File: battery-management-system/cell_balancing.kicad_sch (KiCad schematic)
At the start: 30 parts, among them J22 BALANCE_INPUTS, J23 BALANCE_CURRENT, J27 BALANCE_CONTROL, Q11 DMN3404L, Q12 DMN3730U, Q14 DMN3730U, Q15 DMN3730U, Q16 DMN3730U, Q17 DMN3730U, SW1 CELL1_MINUS, SW2 CELL1_PLUS, SW3 CELL2_MINUS, SW4 CELL2_PLUS, SW5 CELL3_PLUS, SW6 CELL3_MINUS, SW7 CELL4_PLUS, SW8 CELL4_MINUS, U13 MC74VHC139

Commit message: improve layout
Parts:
- renumbered C33 to C45, C30 to C46, C31 to C47, C32 to C48, D16 to D22, D17 to D23, D18 to D24, D19 to D25, J27 to J26, J22 to J27, J23 to J28, Q12 to Q14, Q11 to Q15, Q14 to Q16, Q15 to Q17, Q16 to Q18, Q17 to Q19, R50 to R61, R49 to R62, R48 to R63, SW7 to SW1, SW8 to SW2, SW5 to SW3, SW6 to SW4, SW4 to SW5, SW3 to SW6, SW2 to SW7, SW1 to SW8, U13 to U16

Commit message: add project for DC DC converter PCB
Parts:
- C46, C47, C48: RS order number 875-6720 -> 875-6720
- Q15: RS order number 751-4171 -> 751-4171
- R63: RS order number 796-2431 -> 796-2431
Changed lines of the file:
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@@
       (effects (font (size 1.27 1.27)) hide)
     )
-    (property "RS order number" " 796-2431" (at 160.02 137.16 0)
+    (property "RS order number" "796-2431" (at 160.02 137.16 0)
       (effects (font (size 1.27 1.27)) hide)
     )
@@
       (effects (font (size 1.27 1.27)) hide)
     )
-    (property "RS order number" "    875-6720" (at 238.506 146.05 0)
+    (property "RS order number" "875-6720" (at 238.506 146.05 0)
       (effects (font (size 1.27 1.27)) hide)
     )
@@
       (effects (font (size 1.27 1.27)) hide)
     )
-    (property "RS order number" " 751-4171" (at 156.21 140.97 0)
+    (property "RS order number" "751-4171" (at 156.21 140.97 0)
       (effects (font (size 1.27 1.27)) hide)
     )
@@
       (effects (font (size 1.27 1.27)) hide)
     )
-    (property "RS order number" "    875-6720" (at 263.906 146.05 0)
+    (property "RS order number" "875-6720" (at 263.906 146.05 0)
       (effects (font (size 1.27 1.27)) hide)
     )
@@
       (effects (font (size 1.27 1.27)) hide)
     )
-    (property "RS order number" "    875-6720" (at 251.206 146.05 0)
-      (effects (font (size 1.27 1.27)) hide)
-    )
+    (property "RS order number" "875-6720" (at 251.206 146.05 0)
+      (effects (font (size 1.27 1.27)) hide)
+    )

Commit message: update footprints and layout
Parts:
- removed C48: 90F, benediktibk:vishay_super_cap_form_g, symbol benediktibk:C_90F_THT_4_2V
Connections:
- net BALANCE_CAP_MINUS_RAW: now also C46.2, C47.2; no longer C46.1, C47.1
- net BALANCE_CAP_PLUS_RAW: now also C46.1, C47.1; no longer C46.2, C46.3, C47.2, C47.3
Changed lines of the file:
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@@
 (kicad_sch (version 20230121) (generator eeschema)
   (paper "A4")
-  (junction (at 234.95 137.16) (diameter 0) (color 0 0 0 0)
-  )
   (junction (at 87.63 154.94) (diameter 0) (color 0 0 0 0)
   )
   (junction (at 44.45 80.01) (diameter 0) (color 0 0 0 0)
   )
-  (junction (at 246.38 154.94) (diameter 0) (color 0 0 0 0)
-  )
   (junction (at 194.31 154.94) (diameter 0) (color 0 0 0 0)
   )
@@
   (junction (at 247.65 109.22) (diameter 0) (color 0 0 0 0)
   )
-  (junction (at 222.25 137.16) (diameter 0) (color 0 0 0 0)
-  )
   (junction (at 201.93 154.94) (diameter 0) (color 0 0 0 0)
   )
@@
   (junction (at 222.25 25.4) (diameter 0) (color 0 0 0 0)
   )
-  (junction (at 219.71 137.16) (diameter 0) (color 0 0 0 0)
-  )
   (junction (at 100.33 137.16) (diameter 0) (color 0 0 0 0)
   )
@@
   (junction (at 222.25 19.05) (diameter 0) (color 0 0 0 0)
   )
-  (junction (at 247.65 137.16) (diameter 0) (color 0 0 0 0)
+  (junction (at 220.98 137.16) (diameter 0) (color 0 0 0 0)
   )
   (junction (at 130.81 120.65) (diameter 0) (color 0 0 0 0)
@@
   (junction (at 171.45 154.94) (diameter 0) (color 0 0 0 0)
   )
-  (junction (at 245.11 137.16) (diameter 0) (color 0 0 0 0)
+  (junction (at 233.68 137.16) (diameter 0) (color 0 0 0 0)
   )
   (junction (at 247.65 60.96) (diameter 0) (color 0 0 0 0)
-  )
-  (junction (at 232.41 137.16) (diameter 0) (color 0 0 0 0)
   )
   (junction (at 97.79 154.94) (diameter 0) (color 0 0 0 0)
@@
   (no_connect (at 220.98 74.93))
   (no_connect (at 220.98 69.85))
-  (wire (pts (xy 234.95 137.16) (xy 234.95 143.51))
-    (stroke (width 0) (type default))
-  )
   (wire (pts (xy 67.31 34.29) (xy 67.31 38.1))
     (stroke (width 0) (type default))
@@
     (stroke (width 0) (type default))
   )
-  (wire (pts (xy 246.38 154.94) (xy 255.27 154.94))
+  (wire (pts (xy 233.68 154.94) (xy 255.27 154.94))
+    (stroke (width 0) (type default))
+  )
+  (wire (pts (xy 220.98 137.16) (xy 220.98 143.51))
+    (stroke (width 0) (type default))
+  )
+  (wire (pts (xy 233.68 137.16) (xy 255.27 137.16))
     (stroke (width 0) (type default))
   )
@@
     (stroke (width 0) (type default))
   )
-  (wire (pts (xy 245.11 137.16) (xy 234.95 137.16))
-    (stroke (width 0) (type default))
-  )
-  (wire (pts (xy 222.25 137.16) (xy 222.25 143.51))
-    (stroke (width 0) (type default))
-  )
-  (wire (pts (xy 247.65 137.16) (xy 247.65 143.51))
-    (stroke (width 0) (type default))
-  )
   (wire (pts (xy 194.31 69.85) (xy 200.66 69.85))
     (stroke (width 0) (type default))
@@
     (stroke (width 0) (type default))
   )
-  (wire (pts (xy 246.38 151.13) (xy 246.38 154.94))
-    (stroke (width 0) (type default))
-  )
   (wire (pts (xy 95.25 137.16) (xy 100.33 137.16))
     (stroke (width 0) (type default))
   )
-  (wire (pts (xy 245.11 137.16) (xy 245.11 143.51))
-    (stroke (width 0) (type default))
-  )
   (wire (pts (xy 67.31 53.34) (xy 67.31 57.15))
     (stroke (width 0) (type default))
@@
     (stroke (width 0) (type default))
   )
+  (wire (pts (xy 233.68 137.16) (xy 233.68 143.51))
+    (stroke (width 0) (type default))
+  )
   (wire (pts (xy 44.45 99.06) (xy 44.45 80.01))
     (stroke (width 0) (type default))
@@
     (stroke (width 0) (type default))
   )
-  (wire (pts (xy 232.41 137.16) (xy 222.25 137.16))
-    (stroke (width 0) (type default))
-  )
   (wire (pts (xy 147.32 25.4) (xy 182.88 25.4))
     (stroke (width 0) (type default))
   )
-  (wire (pts (xy 234.95 137.16) (xy 232.41 137.16))
-    (stroke (width 0) (type default))
-  )
   (wire (pts (xy 226.06 64.77) (xy 226.06 115.57))
     (stroke (width 0) (type default))
   )
+  (wire (pts (xy 220.98 137.16) (xy 233.68 137.16))
+    (stroke (width 0) (type default))
+  )
   (wire (pts (xy 72.39 22.86) (xy 100.33 22.86))
     (stroke (width 0) (type default))
@@
     (stroke (width 0) (type default))
   )
-  (wire (pts (xy 255.27 137.16) (xy 247.65 137.16))
-    (stroke (width 0) (type default))
-  )
   (wire (pts (xy 210.82 38.1) (xy 210.82 53.34))
     (stroke (width 0) (type default))
@@
     (stroke (width 0) (type default))
   )
-  (wire (pts (xy 100.33 137.16) (xy 219.71 137.16))
-    (stroke (width 0) (type default))
-  )
-  (wire (pts (xy 219.71 137.16) (xy 219.71 143.51))
+  (wire (pts (xy 100.33 137.16) (xy 220.98 137.16))
     (stroke (width 0) (type default))
   )
@@
     (stroke (width 0) (type default))
   )
-  (wire (pts (xy 232.41 137.16) (xy 232.41 143.51))
-    (stroke (width 0) (type default))
-  )
-  (wire (pts (xy 247.65 137.16) (xy 245.11 137.16))
-    (stroke (width 0) (type default))
-  )
   (wire (pts (xy 161.29 111.76) (xy 143.51 111.76))
     (stroke (width 0) (type default))
@@
     (stroke (width 0) (type default))
   )
-  (wire (pts (xy 219.71 137.16) (xy 222.25 137.16))
-    (stroke (width 0) (type default))
-  )
   (wire (pts (xy 90.17 99.06) (xy 90.17 137.16))
     (stroke (width 0) (type default))
@@
   )
   (wire (pts (xy 200.66 67.31) (xy 189.23 67.31))
-    (stroke (width 0) (type default))
-  )
-  (wire (pts (xy 233.68 154.94) (xy 246.38 154.94))
     (stroke (width 0) (type default))
   )
@@
     (effects (font (size 1.27 1.27)) (justify right))
   )
-  (netclass_flag "" (length 2.54) (shape round) (at 215.9 154.94 0) (fields_autoplaced)
-    (effects (font (size 1.27 1.27)) (justify left bottom))
-    (property "Netclass" "1A" (at 216.5985 152.4 0)
-      (effects (font (size 1.27 1.27) italic) (justify left))
-    )
-  )
   (netclass_flag "" (length 2.54) (shape round) (at 142.24 154.94 0) (fields_autoplaced)
     (effects (font (size 1.27 1.27)) (justify left bottom))
     (property "Netclass" "1A" (at 142.9385 152.4 0)
-      (effects (font (size 1.27 1.27) italic) (justify left))
-    )
-  )
-  (netclass_flag "" (length 2.54) (shape round) (at 214.63 137.16 0) (fields_autoplaced)
-    (effects (font (size 1.27 1.27)) (justify left bottom))
-    (property "Netclass" "1A" (at 215.3285 134.62 0)
       (effects (font (size 1.27 1.27) italic) (justify left))
     )
@@
     (effects (font (size 1.27 1.27)) (justify right bottom))
     (property "Netclass" "CONTROL_SIGNAL" (at 262.3185 87.63 0)
-      (effects (font (size 1.27 1.27) italic) (justify left))
-    )
-  )
-  (netclass_flag "" (length 2.54) (shape round) (at 184.15 154.94 0) (fields_autoplaced)
-    (effects (font (size 1.27 1.27)) (justify left bottom))
-    (property "Netclass" "1A" (at 184.8485 152.4 0)
       (effects (font (size 1.27 1.27) italic) (justify left))
     )
@@
       (effects (font (size 1.27 1.27)) hide)
     )
-    (pin "3")
     (pin "1")
     (pin "2")
@@
     )
   )
-  (symbol (lib_id "benediktibk:C_90F_THT_4_2V") (at 246.38 147.32 0) (unit 1)
-    (in_bom yes) (on_board yes) (dnp no) (fields_autoplaced)
-    (property "Reference" "C48" (at 251.46 144.907 0)
-      (effects (font (size 1.27 1.27)) (justify left))
-    )
-    (property "Value" "90F" (at 251.46 147.447 0)
-      (effects (font (size 1.27 1.27)) (justify left))
-    )
-    (property "Footprint" "benediktibk:vishay_super_cap_form_g" (at 247.3452 151.13 0)
-      (effects (font (size 1.27 1.27)) hide)
-    )
-    (property "Datasheet" "~" (at 246.38 147.32 0)
-      (effects (font (size 1.27 1.27)) hide)
-    )
-    (property "RS order number" "875-6720" (at 263.906 146.05 0)
-      (effects (font (size 1.27 1.27)) hide)
-    )
-    (pin "3")
-    (pin "1")
-    (pin "2")
-    (instances
-      (project "battery-management-system"
-        (path "/5272f0ff-3069-41a9-bca2-80beede8b4b2/3d1b4e38-a765-486c-a970-a0d54d5b41d9"
-          (reference "C48") (unit 1)
-        )
-      )
-    )
-  )
   (symbol (lib_id "benediktibk:SIL05-1A72-BV669") (at 67.31 137.16 0) (unit 1)
     (in_bom yes) (on_board yes) (dnp no)
@@
       (effects (font (size 1.27 1.27)) hide)
     )
-    (pin "3")
-    (pin "1")
-    (pin "2")
+    (pin "1")
+    (pin "2")

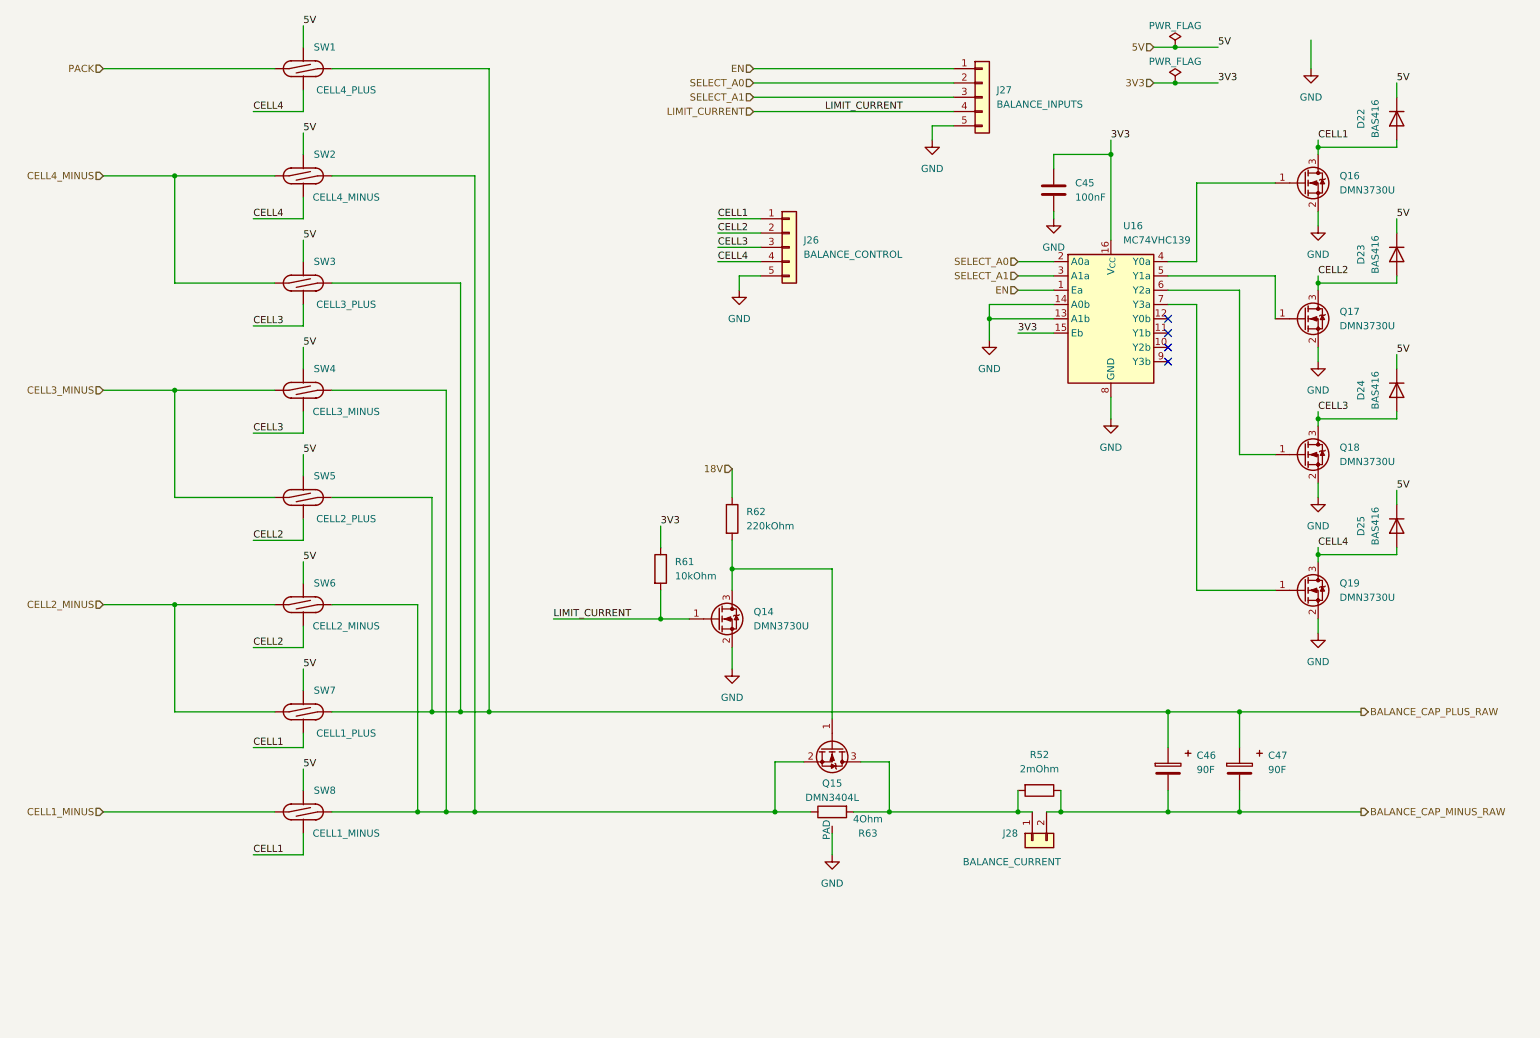
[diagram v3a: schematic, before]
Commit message: switch to inductor based cell balancing
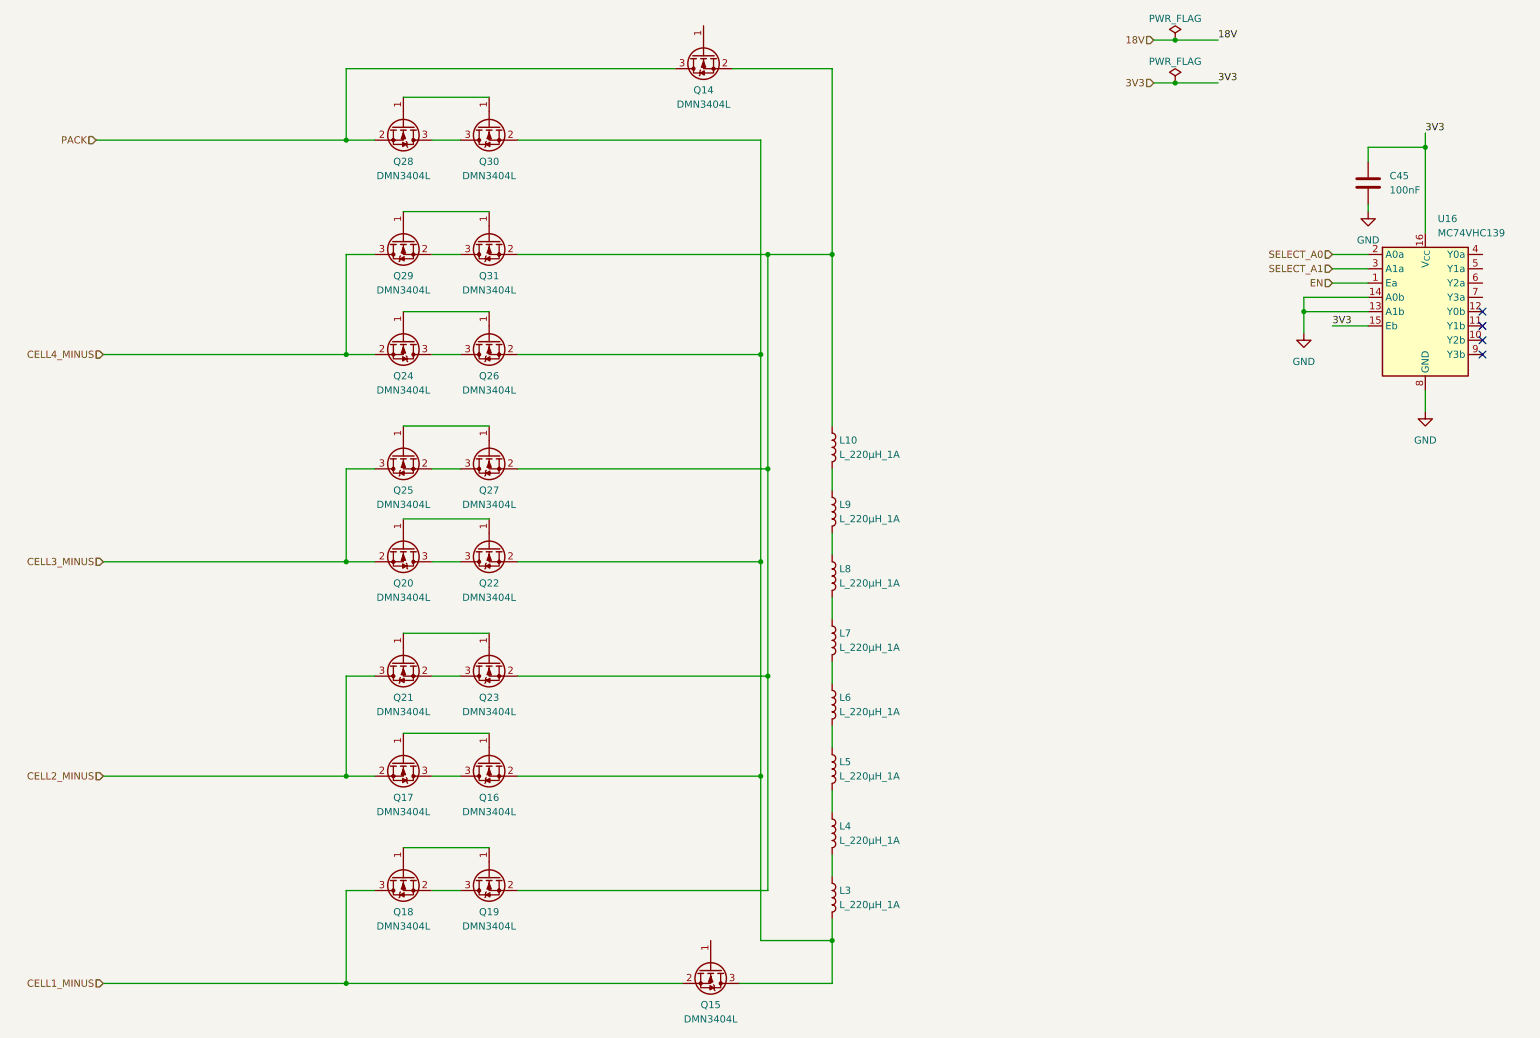
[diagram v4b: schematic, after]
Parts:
- removed C46, C47: 90F, benediktibk:vishay_super_cap_form_g, symbol benediktibk:C_90F_THT_4_2V
- removed D22, D23, D24, D25: BAS416, benediktibk:D_SOD-323, symbol benediktibk:BAS416
- removed J26: BALANCE_CONTROL, benediktibk:PinHeader_1x05_P2.54mm_Vertical, symbol benediktibk:Conn_01x05
- removed J27: BALANCE_INPUTS, benediktibk:PinHeader_1x05_P2.54mm_Vertical, symbol benediktibk:Conn_01x05
- removed J28: BALANCE_CURRENT, benediktibk:PinHeader_1x02_P2.54mm_Vertical, symbol benediktibk:Conn_01x02
- removed Q14, Q16, Q17, Q18, Q19: DMN3730U, benediktibk:SOT-23, symbol benediktibk:DMN3730U
- removed R52: 2mOhm, benediktibk:R_2512_6332Metric_Pad1.40x3.35mm_HandSolder, symbol benediktibk:R_2mOhm_SMD_2512_5W_1%
- removed R61: 10kOhm, benediktibk:R_0603_1608Metric_Pad0.98x0.95mm_HandSolder, symbol benediktibk:R_10kOhm_SMD_0603_100mW_1%
- removed R62: 220kOhm, benediktibk:R_0603_1608Metric_Pad0.98x0.95mm_HandSolder, symbol benediktibk:R_220kOhm_SMD_0603_100mW_1%
- removed R63: 4Ohm, benediktibk:TO-263-resistor, symbol benediktibk:R_4Ohm_SMD_35W_1%
- removed SW1: CELL4_PLUS, benediktibk:SIL05-1A72-BV669, symbol benediktibk:SIL05-1A72-BV669
- removed SW2: CELL4_MINUS, benediktibk:SIL05-1A72-BV669, symbol benediktibk:SIL05-1A72-BV669
- removed SW3: CELL3_PLUS, benediktibk:SIL05-1A72-BV669, symbol benediktibk:SIL05-1A72-BV669
- removed SW4: CELL3_MINUS, benediktibk:SIL05-1A72-BV669, symbol benediktibk:SIL05-1A72-BV669
- removed SW5: CELL2_PLUS, benediktibk:SIL05-1A72-BV669, symbol benediktibk:SIL05-1A72-BV669
- removed SW6: CELL2_MINUS, benediktibk:SIL05-1A72-BV669, symbol benediktibk:SIL05-1A72-BV669
- removed SW7: CELL1_PLUS, benediktibk:SIL05-1A72-BV669, symbol benediktibk:SIL05-1A72-BV669
- removed SW8: CELL1_MINUS, benediktibk:SIL05-1A72-BV669, symbol benediktibk:SIL05-1A72-BV669
- added L10, L3, L4, L5, L6, L7, L8, L9: L_220µH_1A, benediktibk:L_Wuerth_HCI-1050, symbol benediktibk:L_220µH_1A
- added Q14, Q16, Q17, Q18, Q19, Q20, Q21, Q22, Q23, Q24, Q25, Q26, Q27, Q28, Q29, Q30, Q31: DMN3404L, benediktibk:SOT-23, symbol benediktibk:DMN3404L
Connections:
- net CELL1_MINUS: now also Q15.2 (S), Q18.3 (D)
- net CELL2_MINUS: now also Q17.2 (S), Q21.3 (D)
- net CELL3_MINUS: now also Q20.2 (S), Q25.3 (D)
- net CELL4_MINUS: now also Q24.2 (S), Q29.3 (D)
- net PACK: now also Q14.3 (D), Q28.2 (S)
- net at Q15.3 (D): now also L3.2, Q16.2 (S), Q22.2 (S), Q26.2 (S), Q30.2 (S)
- new net: Q29.1 (G), Q31.1 (G)
- new net: L10.1, Q14.2 (S), Q19.2 (S), Q23.2 (S), Q27.2 (S), Q31.2 (S)
- new net: Q29.2 (S), Q31.3 (D)
- new net: Q21.1 (G), Q23.1 (G)
- new net: Q21.2 (S), Q23.3 (D)
- new net: L10.2, L9.1
- new net: L8.1, L9.2
- new net: L7.1, L8.2
- new net: Q20.1 (G), Q22.1 (G)
- new net: Q20.3 (D), Q22.3 (D)
- new net: Q24.1 (G), Q26.1 (G)
- new net: Q24.3 (D), Q26.3 (D)
- new net: Q28.1 (G), Q30.1 (G)
- new net: Q28.3 (D), Q30.3 (D)
- new net: L3.1, L4.2
- new net: Q18.1 (G), Q19.1 (G)
- new net: Q18.2 (S), Q19.3 (D)
- new net: L6.1, L7.2
- new net: L5.1, L6.2
- new net: Q25.1 (G), Q27.1 (G)
- new net: Q25.2 (S), Q27.3 (D)
- new net: L4.1, L5.2
- new net: Q16.1 (G), Q17.1 (G)
- new net: Q16.3 (D), Q17.3 (D)
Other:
- moved on the sheet: C45, U16
